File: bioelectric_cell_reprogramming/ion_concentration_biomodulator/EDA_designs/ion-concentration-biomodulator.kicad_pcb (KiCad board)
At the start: 4 copper layers, 79.6 x 79.4 mm, 49 parts, among them J1 532610671, J10 39-53-2045, J11 Conn_01x14_Pin, J12 Conn_01x14_Pin, J13 39-53-2045, J14 39-53-2045, J15 Conn_ARM_SWD_TagConnect_TC2030, J16 IPL1-104-01-L-D-K, J17 Conn_01x02_Pin, J18 EJ508A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

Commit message: finished v7 (cleared by DRC)
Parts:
- moved U3 0.18 mm to (117.9, 108.9)
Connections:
- U1 pad 30: /USART1_TX -> unconnected-(U1-PA9-Pad30)
- U1 pad 31: /USART1_RX -> unconnected-(U1-PA10-Pad31)
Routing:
- net +5V: track 148.7 -> 187.3 mm, vias 7 -> 10

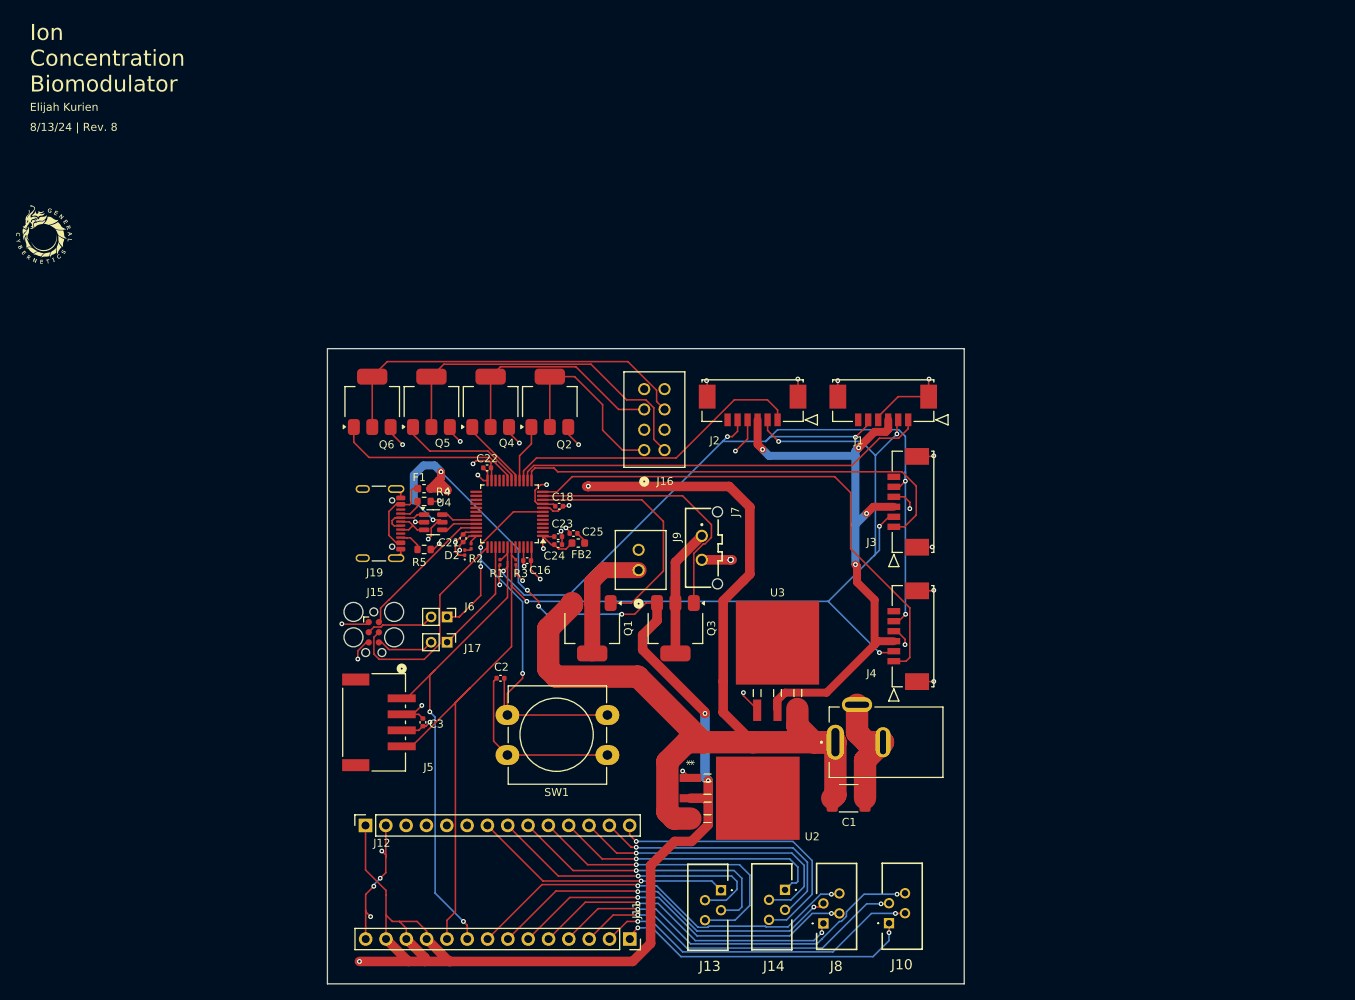
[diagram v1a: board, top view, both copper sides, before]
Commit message: V7 fix: Increased area to add mounting holes and pushed receptacles to the edge of board
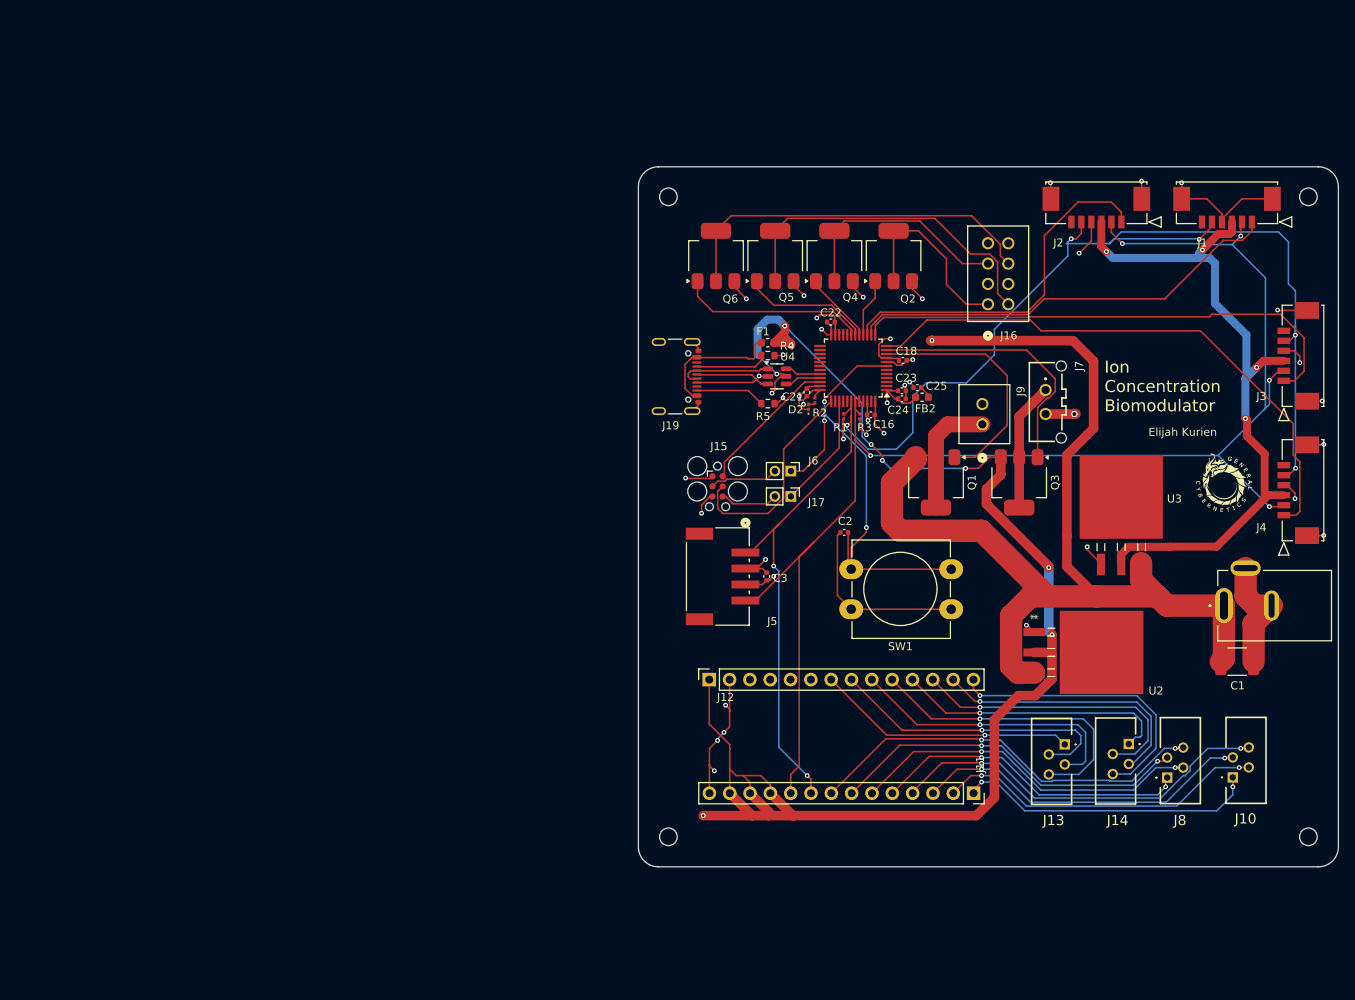
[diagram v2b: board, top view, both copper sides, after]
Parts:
- added H1: MountingHole, MountingHole:MountingHole_2.2mm_M2, F.Cu at (104.2, 133.0)
- added H2: MountingHole, MountingHole:MountingHole_2.2mm_M2, F.Cu at (104.2, 53.0)
- added H3: MountingHole, MountingHole:MountingHole_2.2mm_M2, F.Cu at (184.2, 133.0)
- added H4: MountingHole, MountingHole:MountingHole_2.2mm_M2, F.Cu at (184.2, 53.0)
- F1: value Fuse -> 500mA
- moved G*** 150.7 mm to (173.7, 89.0)
- moved J3 52.1 mm to (181.2, 76.0)
- moved J4 52.1 mm to (181.2, 92.8)
- moved J18 51.5 mm to (176.4, 104.1)
- moved C1 51.5 mm to (175.3, 111.1)
- moved J1 49.6 mm to (177.2, 56.2)
- moved J2 49.6 mm to (160.8, 56.2)
- moved C25 46.7 mm to (135.3, 76.9)
- moved J13 46.7 mm to (153.8, 121.5)
- moved J14 46.7 mm to (161.8, 121.4)
- moved J15 46.7 mm to (110.4, 89.2)
- moved U3 46.7 mm to (160.8, 90.7)
- moved C16 46.7 mm to (129.5, 80.3)
- moved C18 46.7 mm to (133.5, 73.5)
- moved C2 46.7 mm to (126.2, 95.0)
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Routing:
- net /I2C_SCK: track 168.2 -> 188.1 mm
- net +3.3V: track 110.0 -> 126.1 mm
- net /I2C_SDA: track 164.8 -> 179.0 mm
- net Net-(J19-D+-PadA6): track 4.68 -> 16.8 mm
- net /IRQn4: track 38.4 -> 45.4 mm
- net GND: track 133.0 -> 139.4 mm, vias 29 -> 28
- net /IRQn2: track 57.4 -> 63.7 mm
- net Net-(F1-Pad1): track 10.7 -> 16.8 mm
- net Net-(J19-CC2): track 2.83 -> 8.73 mm
- net Net-(J19-CC1): track 2.90 -> 8.79 mm
- net Net-(J19-D--PadA7): track 6.09 -> 12.0 mm
- net /IRQn1: track 66.0 -> 71.1 mm
- net +12V: track 143.3 -> 146.9 mm
- net /IRQn3: track 52.0 -> 54.7 mm
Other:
- board size 79.6 x 79.4 mm -> 87.5 x 87.5 mm
- board text removed: "8/13/24 | Rev. 8"

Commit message: Fix: Pulled out the
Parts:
- moved J8 5.40 mm to (169.9, 121.4), turned to -90 degrees
- moved J10 5.22 mm to (178.0, 121.5), turned to -90 degrees
- moved C3 5.11 mm to (111.4, 100.5)
- moved J5 5.11 mm to (105.3, 100.5)
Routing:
- net /42-: track 37.7 -> 47.8 mm, vias 2 -> 1
- net /32-: track 39.7 -> 49.7 mm, vias 2 -> 1
- net /42+: track 41.4 -> 50.2 mm, vias 2 -> 1
- net /32+: track 44.2 -> 50.9 mm, vias 2 -> 1
- net /I2C_SCK: track 188.1 -> 192.7 mm
- net /41+: track 42.8 -> 47.0 mm, vias 2 -> 1
- net /31+: track 45.4 -> 49.0 mm, vias 2 -> 1
- net /I2C_SDA: track 179.0 -> 181.9 mm
- net /41-: track 48.5 -> 45.9 mm, vias 2 -> 1
- net /31-: track 50.8 -> 48.7 mm, vias 2 -> 1
